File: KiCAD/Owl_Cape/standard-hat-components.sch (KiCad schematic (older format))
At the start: 18 parts, among them Q1 MMDT5401, Q2 DMG2302U, U1 AT24C256C

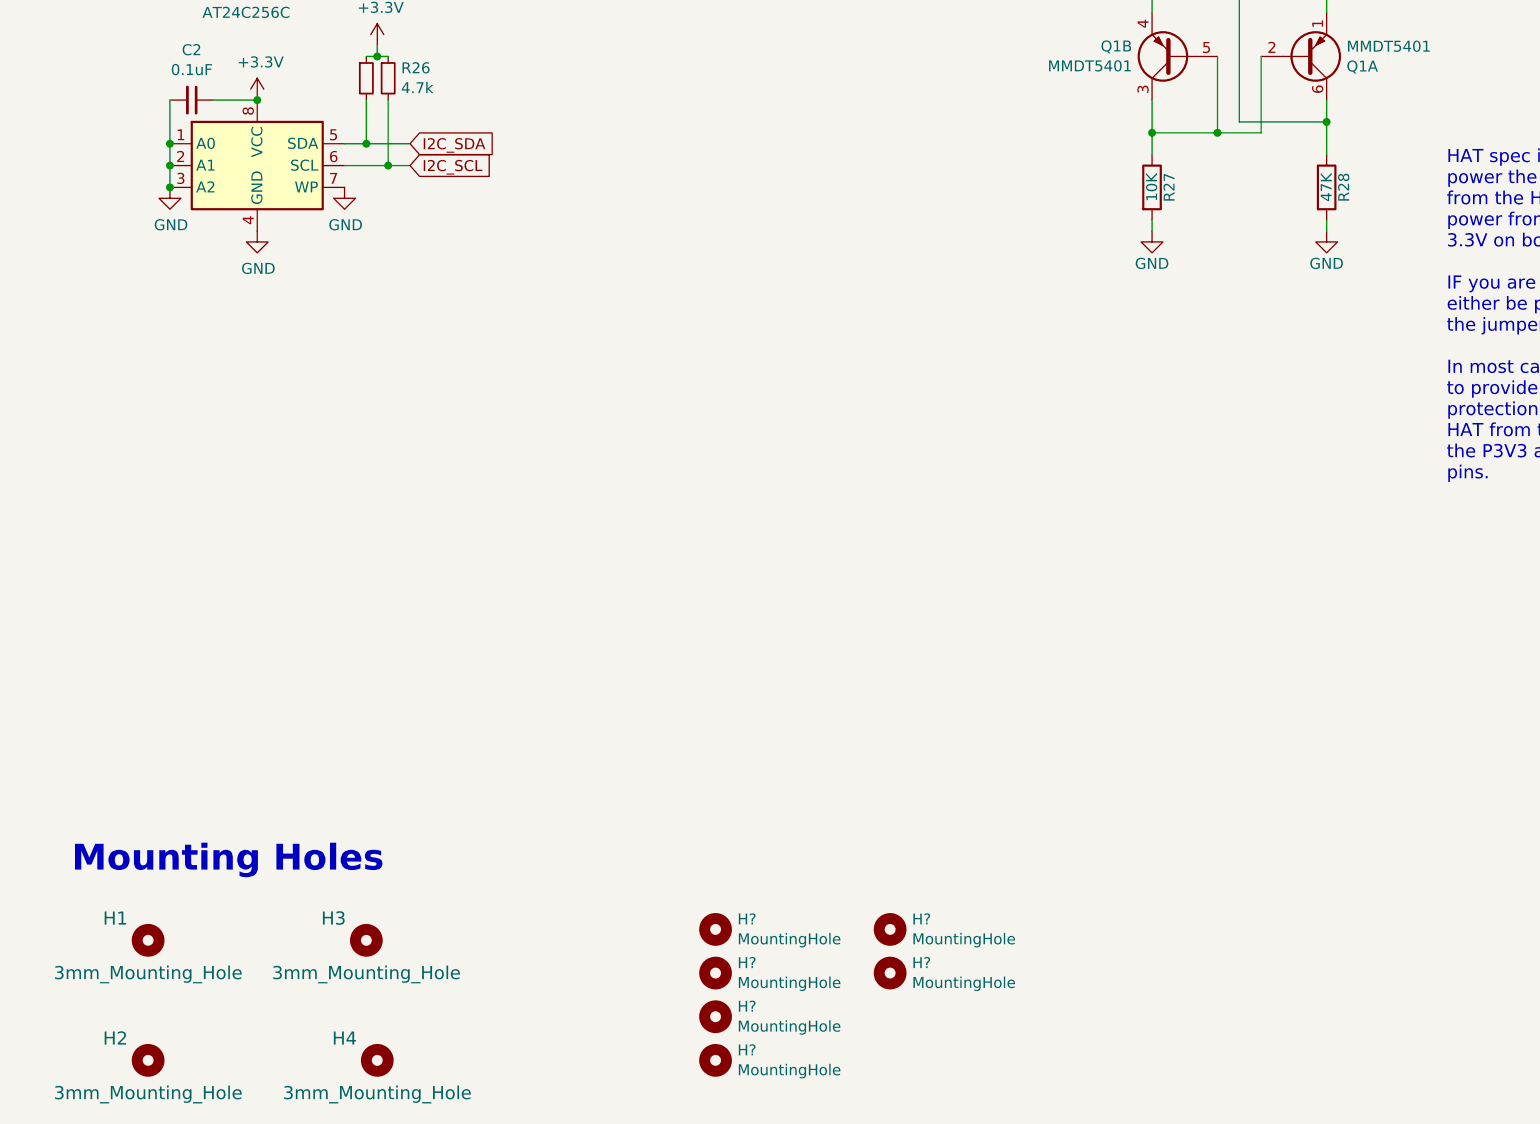
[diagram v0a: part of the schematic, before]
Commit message: logo and kicad updates
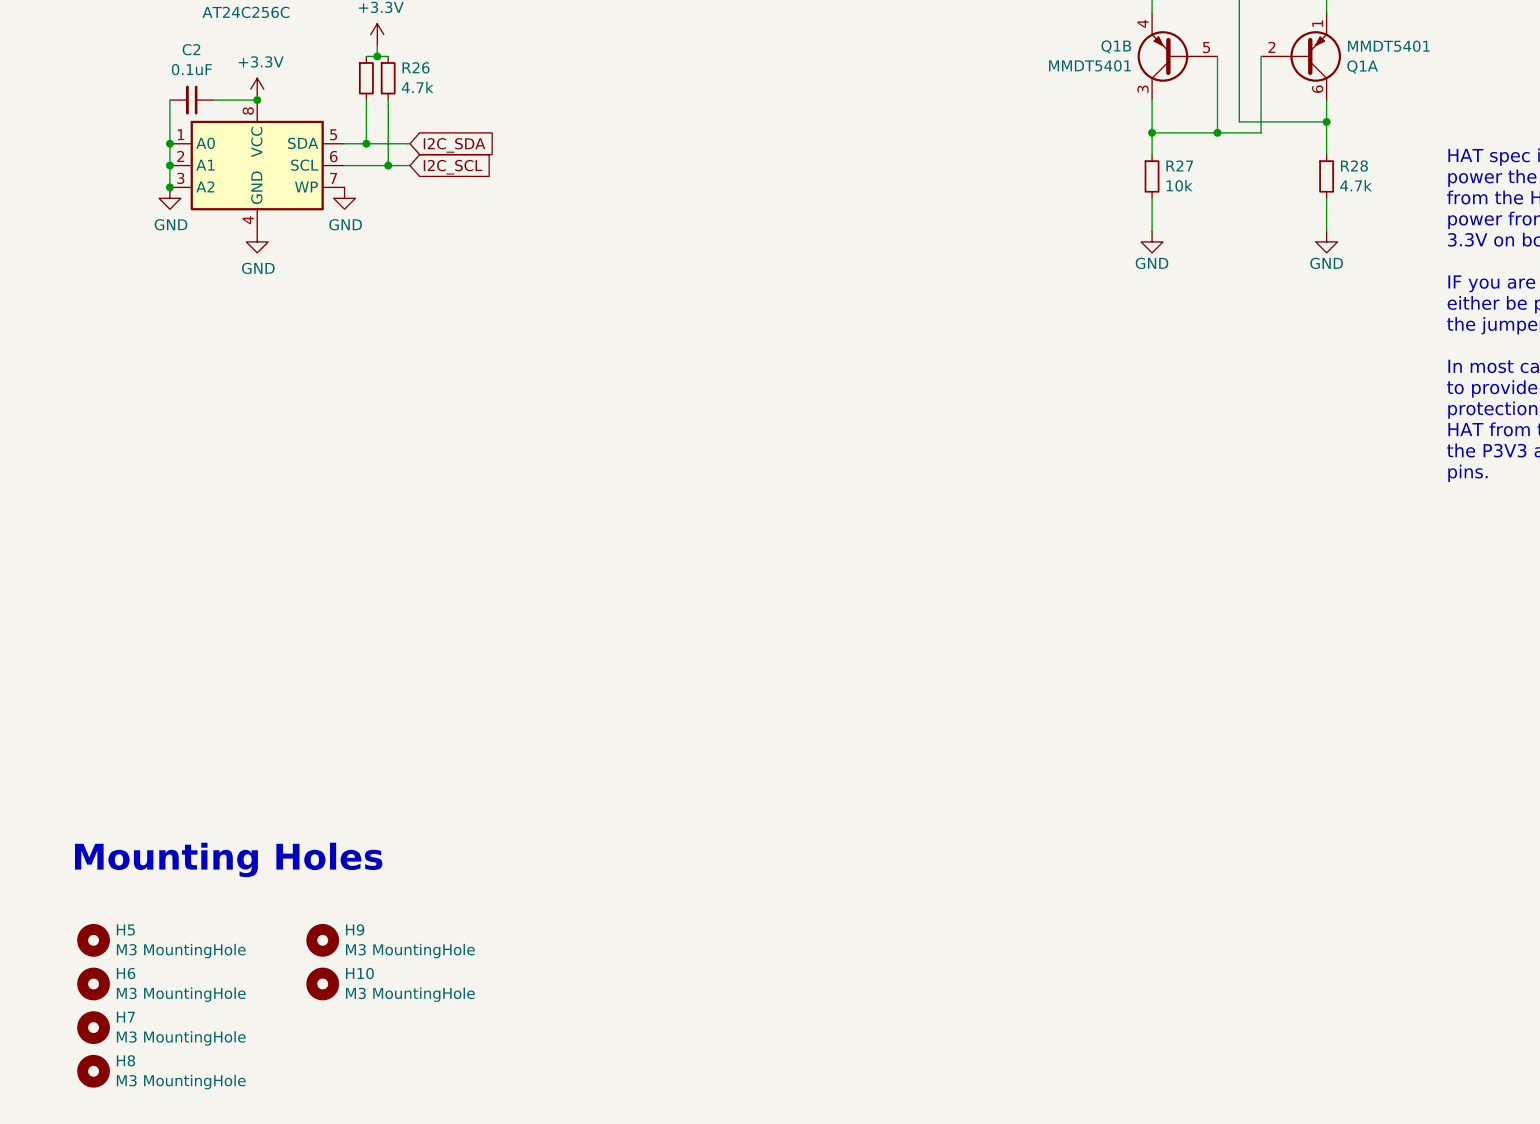
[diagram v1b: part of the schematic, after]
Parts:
- removed H1, H2, H3, H4: 3mm_Mounting_Hole, project_footprints:NPTH_3mm_ID, symbol Mechanical:MountingHole
- removed R27: 10K, Resistor_SMD:R_0603_1608Metric_Pad0.84x1.00mm_HandSolder, symbol Device:R
- removed R28: 47K, Resistor_SMD:R_0603_1608Metric_Pad0.84x1.00mm_HandSolder, symbol Device:R
- added R27: 10k, Resistor_SMD:R_0805_2012Metric, symbol Device:R_Small
- added R28: 4.7k, Resistor_SMD:R_0805_2012Metric, symbol Device:R_Small
- C2: footprint 3544again:C_0805_2012Metric -> Capacitor_SMD:CP_Elec_4x5.3
- H10, H5, H6, H7, H8, H9: renamed from H?; value MountingHole -> M3 MountingHole
- R25, R26: footprint 3544again:R_0805_2012Metric -> Resistor_SMD:R_0805_2012Metric
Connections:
- net GND: now also R27.2, R28.2
- net at Q1.2 (B1), Q1.3 (C2), Q1.5 (B2): now also R27.1
- net at Q1.6 (C1), Q2.1 (G): now also R28.1
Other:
- moved on the sheet: H10, H5, H6, H7, H8, H9
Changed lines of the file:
@@
 encoding utf-8
 Sheet 4 5
-Title ""
+Title "The Owl - RPI Cape 16ch Pixel Controller"
 Date ""
 Rev ""
-Comp ""
+Comp "OnlineDynamic"
 Comment1 ""
 Comment2 ""
@@
 Comment4 ""
 $EndDescr
-$Comp
-L Mechanical:MountingHole H1
-U 1 1 62351E23
-P 1350 6550
-F 0 "H1" H 1200 6650 60  0000 C CNN
-F 1 "3mm_Mounting_Hole" H 1350 6400 60  0000 C CNN
-F 2 "project_footprints:NPTH_3mm_ID" H 1250 6550 60  0001 C CNN
-F 3 "" H 1250 6550 60  0001 C CNN
-	1    1350 6550
-	1    0    0    -1
-$EndComp
-$Comp
-L Mechanical:MountingHole H3
-U 1 1 62351E24
-P 2350 6550
-F 0 "H3" H 2200 6650 60  0000 C CNN
-F 1 "3mm_Mounting_Hole" H 2350 6400 60  0000 C CNN
-F 2 "project_footprints:NPTH_3mm_ID" H 2250 6550 60  0001 C CNN
-F 3 "" H 2250 6550 60  0001 C CNN
-	1    2350 6550
-	1    0    0    -1
-$EndComp
-$Comp
-L Mechanical:MountingHole H2
-U 1 1 5834BD62
-P 1350 7100
-F 0 "H2" H 1200 7200 60  0000 C CNN
-F 1 "3mm_Mounting_Hole" H 1350 6950 60  0000 C CNN
-F 2 "project_footprints:NPTH_3mm_ID" H 1250 7100 60  0001 C CNN
-F 3 "" H 1250 7100 60  0001 C CNN
-	1    1350 7100
-	1    0    0    -1
-$EndComp
-$Comp
-L Mechanical:MountingHole H4
-U 1 1 62351E26
-P 2400 7100
-F 0 "H4" H 2250 7200 60  0000 C CNN
-F 1 "3mm_Mounting_Hole" H 2400 6950 60  0000 C CNN
-F 2 "project_footprints:NPTH_3mm_ID" H 2300 7100 60  0001 C CNN
-F 3 "" H 2300 7100 60  0001 C CNN
-	1    2400 7100
-	1    0    0    -1
-$EndComp
 Text Label 7350 1900 2    60   ~ 0
 P5V_HAT
@@
 Text Notes 5100 1550 0    60   ~ 0
 This is the recommended 5V rail protection for \na HAT with power going to the Pi.\nSee https://github.com/raspberrypi/hats/blob/master/designguide.md#back-powering-the-pi-via-the-j8-gpio-header
-$Comp
-L Device:R R27
-U 1 1 58E15896
-P 5950 3100
-F 0 "R27" V 6030 3100 50  0000 C CNN
-F 1 "10K" V 5950 3100 50  0000 C CNN
-F 2 "Resistor_SMD:R_0603_1608Metric_Pad0.84x1.00mm_HandSolder" V 5880 3100 50  0001 C CNN
-F 3 "" H 5950 3100 50  0001 C CNN
-	1    5950 3100
-	1    0    0    -1
-$EndComp
-$Comp
-L Device:R R28
-U 1 1 58E158A1
-P 6750 3100
-F 0 "R28" V 6830 3100 50  0000 C CNN
-F 1 "47K" V 6750 3100 50  0000 C CNN
-F 2 "Resistor_SMD:R_0603_1608Metric_Pad0.84x1.00mm_HandSolder" V 6680 3100 50  0001 C CNN
-F 3 "" H 6750 3100 50  0001 C CNN
-	1    6750 3100
-	1    0    0    -1
-$EndComp
 $Comp
 L power:GND #PWR056
@@
 	1    0    0    -1
 $EndComp
-Wire Wire Line
-	5950 3300 5950 3250
-Wire Wire Line
-	6750 3300 6750 3250
 Wire Wire Line
 	6750 2700 6750 2800
@@
 F 0 "C2" V 1321 2700 50  0000 C CNN
 F 1 "0.1uF" V 1412 2700 50  0000 C CNN
-F 2 "3544again:C_0805_2012Metric" H 1550 2700 50  0001 C CNN
+F 2 "Capacitor_SMD:CP_Elec_4x5.3" H 1550 2700 50  0001 C CNN
 F 3 "https://datasheet.lcsc.com/szlcsc/Samsung-Electro-Mechanics-CL05B104KO5NNNC_C1525.pdf" H 1550 2700 50  0001 C CNN
 F 4 "C49678" H 1550 2700 50  0001 C CNN "Description"
@@
 F 0 "R26" H 2509 2646 50  0000 L CNN
 F 1 "4.7k" H 2509 2555 50  0000 L CNN
-F 2 "3544again:R_0805_2012Metric" H 2450 2600 50  0001 C CNN
+F 2 "Resistor_SMD:R_0805_2012Metric" H 2450 2600 50  0001 C CNN
 F 3 "https://datasheet.lcsc.com/szlcsc/Uniroyal-Elec-0805W8F2201T5E_C17520.pdf" H 2450 2600 50  0001 C CNN
 F 4 "C17673" H 2450 2600 50  0001 C CNN "Description"
@@
 F 0 "R25" V 2409 2646 50  0001 L CNN
 F 1 "4.7k" H 2409 2555 50  0001 L CNN
-F 2 "3544again:R_0805_2012Metric" H 2350 2600 50  0001 C CNN
+F 2 "Resistor_SMD:R_0805_2012Metric" H 2350 2600 50  0001 C CNN
 F 3 "https://datasheet.lcsc.com/szlcsc/Uniroyal-Elec-0805W8F2201T5E_C17520.pdf" H 2350 2600 50  0001 C CNN
 F 4 "C17673" H 2350 2600 50  0001 C CNN "Description"
@@
 F 0 "U1" H 1800 3800 50  0000 C CNN
 F 1 "AT24C256C" H 1800 3700 50  0000 C CNN
-F 2 "Package_SO:SOIC-8_3.9x4.9mm_P1.27mm" H 1850 3000 50  0001 C CNN
+F 2 "Package_SO:SOIC-8_3.9x4.9mm_P1.27mm" H 1850 3000 50  0001 C BNN
 F 3 "https://www.onsemi.cn/PowerSolutions/document/CAT24C256-D.PDF" H 1850 3000 50  0001 C CNN
 F 4 "C6482" H 1850 3000 50  0001 C CNN "Description"
@@
 EEPROM
 $Comp
-L Mechanical:MountingHole H?
+L Mechanical:MountingHole H5
 U 1 1 623545E3
-P 3950 6500
-F 0 "H?" H 4050 6546 50  0000 L CNN
-F 1 "MountingHole" H 4050 6455 50  0000 L CNN
-F 2 "MountingHole:MountingHole_3.2mm_M3_Pad_TopBottom" H 3950 6500 50  0001 C CNN
-F 3 "~" H 3950 6500 50  0001 C CNN
-	1    3950 6500
-	1    0    0    -1
-$EndComp
-$Comp
-L Mechanical:MountingHole H?
+P 1100 6550
+F 0 "H5" H 1200 6596 50  0000 L CNN
+F 1 "M3 MountingHole" H 1200 6505 50  0000 L CNN
+F 2 "MountingHole:MountingHole_3.2mm_M3_Pad_TopBottom" H 1100 6550 50  0001 C CNN
+F 3 "~" H 1100 6550 50  0001 C CNN
+	1    1100 6550
+	1    0    0    -1
+$EndComp
+$Comp
+L Mechanical:MountingHole H6
 U 1 1 623545E9
-P 3950 6700
-F 0 "H?" H 4050 6746 50  0000 L CNN
-F 1 "MountingHole" H 4050 6655 50  0000 L CNN
-F 2 "MountingHole:MountingHole_3.2mm_M3_Pad_TopBottom" H 3950 6700 50  0001 C CNN
-F 3 "~" H 3950 6700 50  0001 C CNN
-	1    3950 6700
-	1    0    0    -1
-$EndComp
-$Comp
-L Mechanical:MountingHole H?
+P 1100 6750
+F 0 "H6" H 1200 6796 50  0000 L CNN
+F 1 "M3 MountingHole" H 1200 6705 50  0000 L CNN
+F 2 "MountingHole:MountingHole_3.2mm_M3_Pad_TopBottom" H 1100 6750 50  0001 C CNN
+F 3 "~" H 1100 6750 50  0001 C CNN
+	1    1100 6750
+	1    0    0    -1
+$EndComp
+$Comp
+L Mechanical:MountingHole H7
 U 1 1 623545EF
-P 3950 6900
-F 0 "H?" H 4050 6946 50  0000 L CNN
-F 1 "MountingHole" H 4050 6855 50  0000 L CNN
-F 2 "MountingHole:MountingHole_3.2mm_M3_Pad_TopBottom" H 3950 6900 50  0001 C CNN
-F 3 "~" H 3950 6900 50  0001 C CNN
-	1    3950 6900
-	1    0    0    -1
-$EndComp
-$Comp
-L Mechanical:MountingHole H?
+P 1100 6950
+F 0 "H7" H 1200 6996 50  0000 L CNN
+F 1 "M3 MountingHole" H 1200 6905 50  0000 L CNN
+F 2 "MountingHole:MountingHole_3.2mm_M3_Pad_TopBottom" H 1100 6950 50  0001 C CNN
+F 3 "~" H 1100 6950 50  0001 C CNN
+	1    1100 6950
+	1    0    0    -1
+$EndComp
+$Comp
+L Mechanical:MountingHole H8
 U 1 1 623545F5
-P 3950 7100
-F 0 "H?" H 4050 7146 50  0000 L CNN
-F 1 "MountingHole" H 4050 7055 50  0000 L CNN
-F 2 "MountingHole:MountingHole_3.2mm_M3_Pad_TopBottom" H 3950 7100 50  0001 C CNN
-F 3 "~" H 3950 7100 50  0001 C CNN
-	1    3950 7100
-	1    0    0    -1
-$EndComp
-$Comp
-L Mechanical:MountingHole H?
+P 1100 7150
+F 0 "H8" H 1200 7196 50  0000 L CNN
+F 1 "M3 MountingHole" H 1200 7105 50  0000 L CNN
+F 2 "MountingHole:MountingHole_3.2mm_M3_Pad_TopBottom" H 1100 7150 50  0001 C CNN
+F 3 "~" H 1100 7150 50  0001 C CNN
+	1    1100 7150
+	1    0    0    -1
+$EndComp
+$Comp
+L Mechanical:MountingHole H9
 U 1 1 623545FB
-P 4750 6500
-F 0 "H?" H 4850 6546 50  0000 L CNN
-F 1 "MountingHole" H 4850 6455 50  0000 L CNN
-F 2 "MountingHole:MountingHole_3.2mm_M3_Pad_TopBottom" H 4750 6500 50  0001 C CNN
-F 3 "~" H 4750 6500 50  0001 C CNN
-	1    4750 6500
-	1    0    0    -1
-$EndComp
-$Comp
-L Mechanical:MountingHole H?
+P 2150 6550
+F 0 "H9" H 2250 6596 50  0000 L CNN
+F 1 "M3 MountingHole" H 2250 6505 50  0000 L CNN
+F 2 "MountingHole:MountingHole_3.2mm_M3_Pad_TopBottom" H 2150 6550 50  0001 C CNN
+F 3 "~" H 2150 6550 50  0001 C CNN
+	1    2150 6550
+	1    0    0    -1
+$EndComp
+$Comp
+L Mechanical:MountingHole H10
 U 1 1 62354601
-P 4750 6700
-F 0 "H?" H 4850 6746 50  0000 L CNN
-F 1 "MountingHole" H 4850 6655 50  0000 L CNN
-F 2 "MountingHole:MountingHole_3.2mm_M3_Pad_TopBottom" H 4750 6700 50  0001 C CNN
-F 3 "~" H 4750 6700 50  0001 C CNN
-	1    4750 6700
-	1    0    0    -1
-$EndComp
+P 2150 6750
+F 0 "H10" H 2250 6796 50  0000 L CNN
+F 1 "M3 MountingHole" H 2250 6705 50  0000 L CNN
+F 2 "MountingHole:MountingHole_3.2mm_M3_Pad_TopBottom" H 2150 6750 50  0001 C CNN
+F 3 "~" H 2150 6750 50  0001 C CNN
+	1    2150 6750
+	1    0    0    -1
+$EndComp
+$Comp
+L Device:R_Small R?
+U 1 1 6237BD5B
+P 6750 3050
+AR Path="/6235D74F/6237BD5B" Ref="R?"  Part="1"
+AR Path="/6235185D/6237BD5B" Ref="R28"  Part="1"
+F 0 "R28" H 6809 3096 50  0000 L CNN
+F 1 "4.7k" H 6809 3005 50  0000 L CNN
+F 2 "Resistor_SMD:R_0805_2012Metric" H 6750 3050 50  0001 C CNN
+F 3 "https://datasheet.lcsc.com/szlcsc/Uniroyal-Elec-0805W8F2201T5E_C17520.pdf" H 6750 3050 50  0001 C CNN
+F 4 "C17673" H 6750 3050 50  0001 C CNN "Description"
+	1    6750 3050
+	1    0    0    -1
+$EndComp
+Wire Wire Line
+	6750 3150 6750 3300
+$Comp
+L Device:R_Small R?
+U 1 1 62380363
+P 5950 3050
+AR Path="/6235D74F/62380363" Ref="R?"  Part="1"
+AR Path="/6235185D/62380363" Ref="R27"  Part="1"
+F 0 "R27" H 6009 3096 50  0000 L CNN
+F 1 "10k" H 6009 3005 50  0000 L CNN
+F 2 "Resistor_SMD:R_0805_2012Metric" H 5950 3050 50  0001 C CNN
+F 3 "https://datasheet.lcsc.com/szlcsc/Uniroyal-Elec-0805W8F2201T5E_C17520.pdf" H 5950 3050 50  0001 C CNN
+F 4 "C17673" H 5950 3050 50  0001 C CNN "Description"
+	1    5950 3050
+	1    0    0    -1
+$EndComp
+Wire Wire Line
+	5950 3150 5950 3300
 $EndSCHEMATC
